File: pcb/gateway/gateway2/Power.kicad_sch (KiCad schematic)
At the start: 12 parts, among them J11 Conn_01x05, U3 RT6150AGQW

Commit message: WIP.
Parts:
- D1: value D_Schottky -> PMEG6010ELRX; footprint (none) -> Diode_SMD:Nexperia_CFP3_SOD-123W
- renumbered C26 to C36, J11 to J3, R13 to R20, R14 to R21, R15 to R22, R25 to R23, R23 to R24, R24 to R25
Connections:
- no-connect marks 0 -> 1

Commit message: WIP.
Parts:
- removed J3: Conn_01x05, symbol Connector_Generic:Conn_01x05
- added D2: PMEG6010ELRX, Diode_SMD:Nexperia_CFP3_SOD-123W, symbol Device:D_Schottky
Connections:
- net VSYS: now also D2.1 (K)
- net VBUS renamed V_USB
- new net V_AUX: D2.2 (A)
- no-connect marks 1 -> 0

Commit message: Starting to look at routing.
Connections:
- net VSYS renamed +5V
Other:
- note removed: "Do I do POE?"
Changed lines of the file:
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@@
 	(generator_version "10.0")
 	(paper "A4")
-	(text "Do I do POE?"
-		(exclude_from_sim no)
-		(at 169.672 57.404 0)
-		(effects
-			(font
-				(size 1.27 1.27)
-				(color 255 0 0 1)
-			)
-		)
-	)
 	(junction
 		(at 171.45 91.44)
@@
 	)
 	(junction
-		(at 138.43 68.58)
-		(diameter 0)
-		(color 0 0 0 0)
-	)
-	(junction
 		(at 133.35 68.58)
 		(diameter 0)
@@
 	)
 	(junction
+		(at 193.04 68.58)
+		(diameter 0)
+		(color 0 0 0 0)
+	)
+	(junction
 		(at 187.96 68.58)
 		(diameter 0)
@@
 	(wire
 		(pts
-			(xy 138.43 62.23) (xy 138.43 68.58)
-		)
-		(stroke
-			(width 0)
-			(type default)
-		)
-	)
-	(wire
-		(pts
 			(xy 107.95 88.9) (xy 107.95 90.17)
 		)
@@
 	(wire
 		(pts
-			(xy 129.54 68.58) (xy 133.35 68.58)
+			(xy 193.04 57.15) (xy 193.04 68.58)
 		)
 		(stroke
@@
 	(wire
 		(pts
-			(xy 107.95 90.17) (xy 107.95 92.71)
+			(xy 129.54 68.58) (xy 133.35 68.58)
 		)
 		(stroke
@@
 	(wire
 		(pts
-			(xy 138.43 68.58) (xy 140.97 68.58)
+			(xy 107.95 90.17) (xy 107.95 92.71)
 		)
 		(stroke
@@
 	(wire
 		(pts
-			(xy 133.35 68.58) (xy 138.43 68.58)
+			(xy 133.35 68.58) (xy 140.97 68.58)
 		)
 		(stroke
@@
 		)
 	)
+	(hierarchical_label "+5V"
+		(shape output)
+		(at 193.04 57.15 90)
+		(effects
+			(font
+				(size 1.27 1.27)
+			)
+			(justify left)
+		)
+	)
 	(hierarchical_label "POWER_SAVE"
 		(shape input)
@@
 		(in_pos_files yes)
 		(dnp no)
-		(fields_autoplaced yes)
 		(property "Reference" "#FLG03"
 			(at 140.97 64.135 0)
@@
 			)
 		)
-		(property "Value" "PWR_FLAG"
-			(at 140.97 60.96 0)
+		(property "Value" "+5V"
+			(at 140.97 62.23 0)
 			(show_name no)
 			(do_not_autoplace no)
@@
 					(unit 1)
 				)
-			)
-		)
-	)
-	(symbol
-		(lib_id "power:VBUS")
-		(at 138.43 62.23 0)
-		(unit 1)
-		(body_style 1)
-		(exclude_from_sim no)
-		(in_bom yes)
-		(on_board yes)
-		(in_pos_files yes)
-		(dnp no)
-		(fields_autoplaced yes)
-		(property "Reference" "#PWR052"
-			(at 138.43 66.04 0)
-			(hide yes)
-			(show_name no)
-			(do_not_autoplace no)
-			(effects
-				(font
-					(size 1.27 1.27)
-				)
-			)
-		)
-		(property "Value" "VSYS"
-			(at 138.43 57.15 0)
-			(show_name no)
-			(do_not_autoplace no)
-			(effects
-				(font
-					(size 1.27 1.27)
-				)
-			)
-		)
-		(property "Footprint" ""
-			(at 138.43 62.23 0)
-			(hide yes)
-			(show_name no)
-			(do_not_autoplace no)
-			(effects
-				(font
-					(size 1.27 1.27)
-				)
-			)
-		)
-		(property "Datasheet" ""
-			(at 138.43 62.23 0)
-			(hide yes)
-			(show_name no)
-			(do_not_autoplace no)
-			(effects
-				(font
-					(size 1.27 1.27)
-				)
-			)
-		)
-		(property "Description" "Power symbol creates a global label with name \"VBUS\""
-			(at 138.43 62.23 0)
-			(hide yes)
-			(show_name no)
-			(do_not_autoplace no)
-			(effects
-				(font
-					(size 1.27 1.27)
-				)
-			)
-		)
-		(pin "1"
-		)
-		(instances
-			(project "gateway2"
-				(path "/1800ee7d-fb6b-47f6-b72a-2ea19411a9d6/68a8a9a9-df38-4ae8-987a-9ba8dce22c75"
-					(reference "#PWR052")
-					(unit 1)
-				)

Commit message: Doing some routing.
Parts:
- L5: footprint Richtek_RT6150:WDFN-10-1EP_3x3mm_P0.5mm_EP1.8x2.5mm -> Abracon_AOTA_B201610S:L_0806_2016Metric
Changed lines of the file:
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@@
 			)
 		)
-		(property "Footprint" "Richtek_RT6150:WDFN-10-1EP_3x3mm_P0.5mm_EP1.8x2.5mm"
+		(property "Footprint" "Abracon_AOTA_B201610S:L_0806_2016Metric"
 			(at 203.2 95.25 0)
 			(hide yes)

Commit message: Moving stuff to proper library.
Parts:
- U3: footprint Richtek_RT6150:WDFN-10-1EP_3x3mm_P0.5mm_EP1.8x2.5mm -> Package_DFN_QFN:WDFN-10-1EP_3x3mm_P0.5mm_EP1.8x2.5mm; symbol Richtek_RT6150:RT6150AGQW -> Regulator_Switching:RT6150AGQW
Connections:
- net GND: now also U3.[3,9] (GND); no longer U3.3 (GND), U3.9 (GND)
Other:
- moved on the sheet: L5, R22, R24, R25, U3

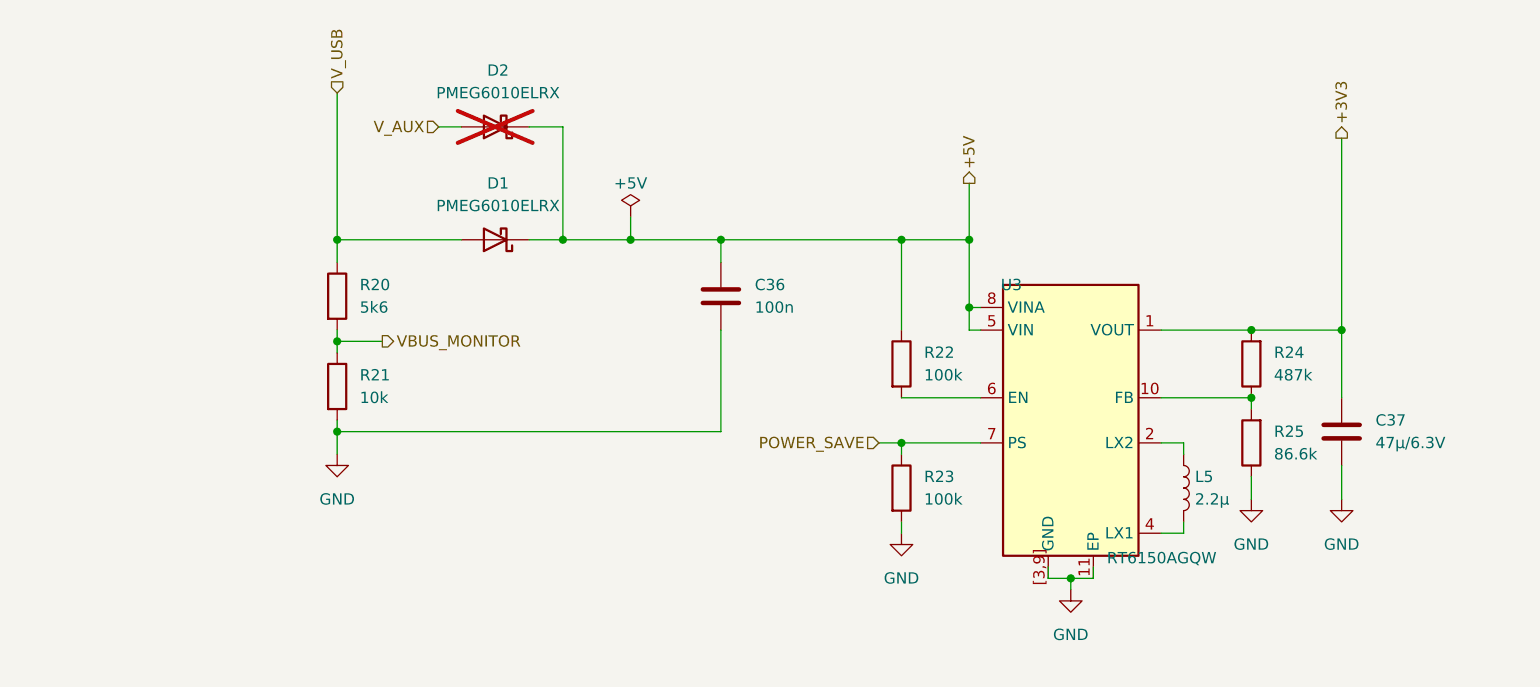
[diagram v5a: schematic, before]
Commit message: Working on power converter.
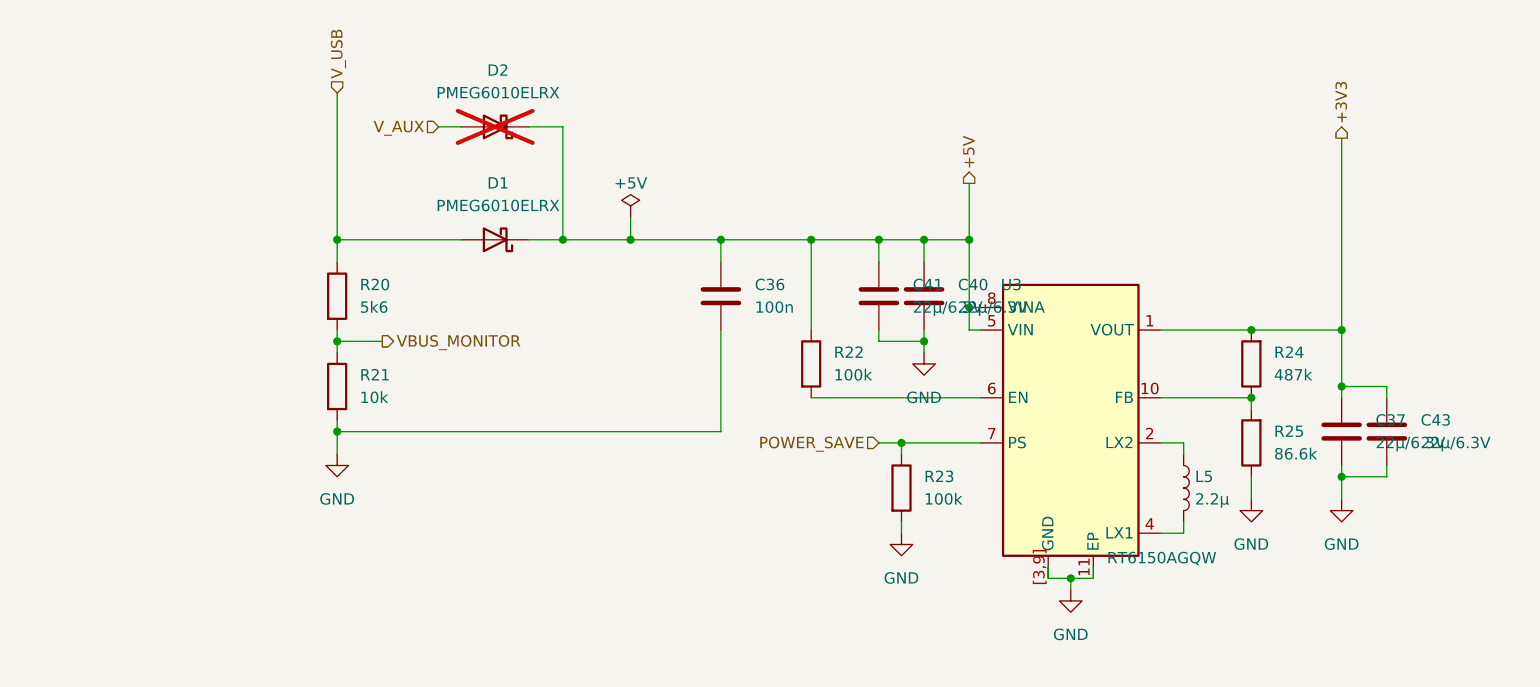
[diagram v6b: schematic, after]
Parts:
- added C40, C41, C43: 22μ/6.3V, Capacitor_SMD:C_1206_3216Metric, symbol Device:C
- C37: value 47μ/6.3V -> 22μ/6.3V; footprint Capacitor_SMD:C_0603_1608Metric -> Capacitor_SMD:C_1206_3216Metric
- L5: footprint Abracon_AOTA_B201610S:L_0806_2016Metric -> Inductor_SMD:L_1206_3216Metric
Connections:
- net +3V3: now also C43.2
- net +5V: now also C40.2, C41.2
- net GND: now also C40.1, C41.1, C43.1
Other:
- moved on the sheet: R22

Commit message: Routing some more.
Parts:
- removed D2: PMEG6010ELRX, Diode_SMD:Nexperia_CFP3_SOD-123W, symbol Device:D_Schottky
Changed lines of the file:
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@@
-	)
-	(junction
-		(at 133.35 68.58)
-		(diameter 0)
-		(color 0 0 0 0)
 	)
 	(junction
@@
 	(wire
 		(pts
-			(xy 129.54 68.58) (xy 133.35 68.58)
+			(xy 129.54 68.58) (xy 140.97 68.58)
 		)
 		(stroke
@@
 	(wire
 		(pts
-			(xy 119.38 55.88) (xy 121.92 55.88)
-		)
-		(stroke
-			(width 0)
-			(type default)
-		)
-	)
-	(wire
-		(pts
 			(xy 173.99 78.74) (xy 173.99 80.01)
 		)
@@
 	(wire
 		(pts
-			(xy 133.35 68.58) (xy 140.97 68.58)
-		)
-		(stroke
-			(width 0)
-			(type default)
-		)
-	)
-	(wire
-		(pts
 			(xy 171.45 100.33) (xy 171.45 101.6)
 		)
@@
 	(wire
 		(pts
-			(xy 133.35 55.88) (xy 133.35 68.58)
-		)
-		(stroke
-			(width 0)
-			(type default)
-		)
-	)
-	(wire
-		(pts
 			(xy 107.95 78.74) (xy 107.95 80.01)
-		)
-		(stroke
-			(width 0)
-			(type default)
-		)
-	)
-	(wire
-		(pts
-			(xy 129.54 55.88) (xy 133.35 55.88)
 		)
 		(stroke
@@
 		)
 	)
-	(hierarchical_label "V_AUX"
-		(shape input)
-		(at 119.38 55.88 180)
-		(effects
-			(font
-				(size 1.27 1.27)
-			)
-			(justify right)
-		)
-	)
 	(hierarchical_label "+5V"
 		(shape output)
@@
 					(unit 1)
 				)
-			)
-		)
-	)
-	(symbol
-		(lib_id "Device:D_Schottky")
-		(at 125.73 55.88 180)
-		(unit 1)
-		(body_style 1)
-		(exclude_from_sim no)
-		(in_bom yes)
-		(on_board yes)
-		(in_pos_files yes)
-		(dnp yes)
-		(fields_autoplaced yes)
-		(property "Reference" "D2"
-			(at 126.0475 49.53 0)
-			(show_name no)
-			(do_not_autoplace no)
-			(effects
-				(font
-					(size 1.27 1.27)
-				)
-			)
-		)
-		(property "Value" "PMEG6010ELRX"
-			(at 126.0475 52.07 0)
-			(show_name no)
-			(do_not_autoplace no)
-			(effects
-				(font
-					(size 1.27 1.27)
-				)
-			)
-		)
-		(property "Footprint" "Diode_SMD:Nexperia_CFP3_SOD-123W"
-			(at 125.73 55.88 0)
-			(hide yes)
-			(show_name no)
-			(do_not_autoplace no)
-			(effects
-				(font
-					(size 1.27 1.27)
-				)
-			)
-		)
-		(property "Datasheet" ""
-			(at 125.73 55.88 0)
-			(hide yes)
-			(show_name no)
-			(do_not_autoplace no)
-			(effects
-				(font
-					(size 1.27 1.27)
-				)
-			)
-		)
-		(property "Description" "Schottky diode"
-			(at 125.73 55.88 0)
-			(hide yes)
-			(show_name no)
-			(do_not_autoplace no)
-			(effects
-				(font
-					(size 1.27 1.27)
-				)
-			)
-		)
-		(pin "2"
-		)
-		(pin "1"
-		)
-		(instances
-			(project "gateway2"
-				(path "/1800ee7d-fb6b-47f6-b72a-2ea19411a9d6/68a8a9a9-df38-4ae8-987a-9ba8dce22c75"
-					(reference "D2")
-					(unit 1)
-				)

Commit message: Still routing.
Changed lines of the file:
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@@
+	)
+	(junction
+		(at 190.5 106.68)
+		(diameter 0)
+		(color 0 0 0 0)
 	)
 	(junction
@@
 	)
 	(junction
-		(at 190.5 106.68)
-		(diameter 0)
-		(color 0 0 0 0)
-	)
-	(junction
 		(at 173.99 80.01)
 		(diameter 0)
@@
 	(wire
 		(pts
-			(xy 187.96 105.41) (xy 187.96 106.68)
+			(xy 190.5 106.68) (xy 190.5 110.49)
+		)
+		(stroke
+			(width 0)
+			(type default)
+		)
+	)
+	(wire
+		(pts
+			(xy 107.95 80.01) (xy 107.95 81.28)
+		)
+		(stroke
+			(width 0)
+			(type default)
+		)
+	)
+	(wire
+		(pts
+			(xy 226.06 95.25) (xy 220.98 95.25)
+		)
+		(stroke
+			(width 0)
+			(type default)
+		)
+	)
+	(wire
+		(pts
+			(xy 226.06 86.36) (xy 226.06 85.09)
+		)
+		(stroke
+			(width 0)
+			(type default)
+		)
+	)
+	(wire
+		(pts
+			(xy 168.91 78.74) (xy 168.91 80.01)
+		)
+		(stroke
+			(width 0)
+			(type default)
+		)
+	)
+	(wire
+		(pts
+			(xy 200.66 86.36) (xy 210.82 86.36)
+		)
+		(stroke
+			(width 0)
+			(type default)
+		)
+	)
+	(wire
+		(pts
+			(xy 210.82 95.25) (xy 210.82 97.79)
+		)
+		(stroke
+			(width 0)
+			(type default)
+		)
+	)
+	(wire
+		(pts
+			(xy 107.95 80.01) (xy 113.03 80.01)
 		)
 		(stroke
@@
 	(wire
 		(pts
-			(xy 190.5 106.68) (xy 190.5 107.95)
-		)
-		(stroke
-			(width 0)
-			(type default)
-		)
-	)
-	(wire
-		(pts
-			(xy 107.95 80.01) (xy 107.95 81.28)
-		)
-		(stroke
-			(width 0)
-			(type default)
-		)
-	)
-	(wire
-		(pts
-			(xy 226.06 95.25) (xy 220.98 95.25)
-		)
-		(stroke
-			(width 0)
-			(type default)
-		)
-	)
-	(wire
-		(pts
-			(xy 226.06 86.36) (xy 226.06 85.09)
-		)
-		(stroke
-			(width 0)
-			(type default)
-		)
-	)
-	(wire
-		(pts
-			(xy 168.91 78.74) (xy 168.91 80.01)
-		)
-		(stroke
-			(width 0)
-			(type default)
-		)
-	)
-	(wire
-		(pts
-			(xy 200.66 86.36) (xy 210.82 86.36)
-		)
-		(stroke
-			(width 0)
-			(type default)
-		)
-	)
-	(wire
-		(pts
-			(xy 210.82 95.25) (xy 210.82 97.79)
-		)
-		(stroke
-			(width 0)
-			(type default)
-		)
-	)
-	(wire
-		(pts
-			(xy 107.95 80.01) (xy 113.03 80.01)
-		)
-		(stroke
-			(width 0)
-			(type default)
-		)
-	)
-	(wire
-		(pts
 			(xy 179.07 62.23) (xy 179.07 68.58)
 		)
@@
 	(wire
 		(pts
-			(xy 193.04 105.41) (xy 193.04 106.68)
-		)
-		(stroke
-			(width 0)
-			(type default)
-		)
-	)
-	(wire
-		(pts
 			(xy 179.07 76.2) (xy 180.34 76.2)
 		)
@@
 	(wire
 		(pts
-			(xy 193.04 106.68) (xy 190.5 106.68)
-		)
-		(stroke
-			(width 0)
-			(type default)
-		)
-	)
-	(wire
-		(pts
 			(xy 140.97 66.04) (xy 140.97 68.58)
 		)
@@
 		(pts
 			(xy 140.97 68.58) (xy 168.91 68.58)
+		)
+		(stroke
+			(width 0)
+			(type default)
+		)
+	)
+	(wire
+		(pts
+			(xy 190.5 106.68) (xy 193.04 106.68)
 		)
 		(stroke
@@
 	(symbol
 		(lib_id "power:GND")
-		(at 190.5 107.95 0)
+		(at 190.5 110.49 0)
 		(unit 1)
 		(body_style 1)
@@
 		(fields_autoplaced yes)
 		(property "Reference" "#PWR054"
-			(at 190.5 114.3 0)
+			(at 190.5 116.84 0)
 			(hide yes)
 			(show_name no)
@@
 		)
 		(property "Value" "GND"
-			(at 190.5 113.03 0)
+			(at 190.5 115.57 0)
 			(show_name no)
 			(do_not_autoplace no)
@@
 		)
 		(property "Footprint" ""
-			(at 190.5 107.95 0)
+			(at 190.5 110.49 0)
 			(hide yes)
 			(show_name no)
@@
 		)
 		(property "Datasheet" ""
-			(at 190.5 107.95 0)
+			(at 190.5 110.49 0)
 			(hide yes)
 			(show_name no)
@@
 		)
 		(property "Description" "Power symbol creates a global label with name \"GND\" , ground"
-			(at 190.5 107.95 0)
+			(at 190.5 110.49 0)
 			(hide yes)
 			(show_name no)
